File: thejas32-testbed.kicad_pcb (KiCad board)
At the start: 4 copper layers, 81.4 x 89.2 mm, 101 parts, among them J1 Conn_01x04, J10 Conn_02x10_Odd_Even, J11 Conn_01x03, J12 Conn_02x20_Odd_Even, J13 Conn_01x03, J2 USB_B_Micro, J3 Conn_02x03_Odd_Even, J4 Conn_02x05_Odd_Even, J5 Conn_01x05, J6 Conn_01x10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

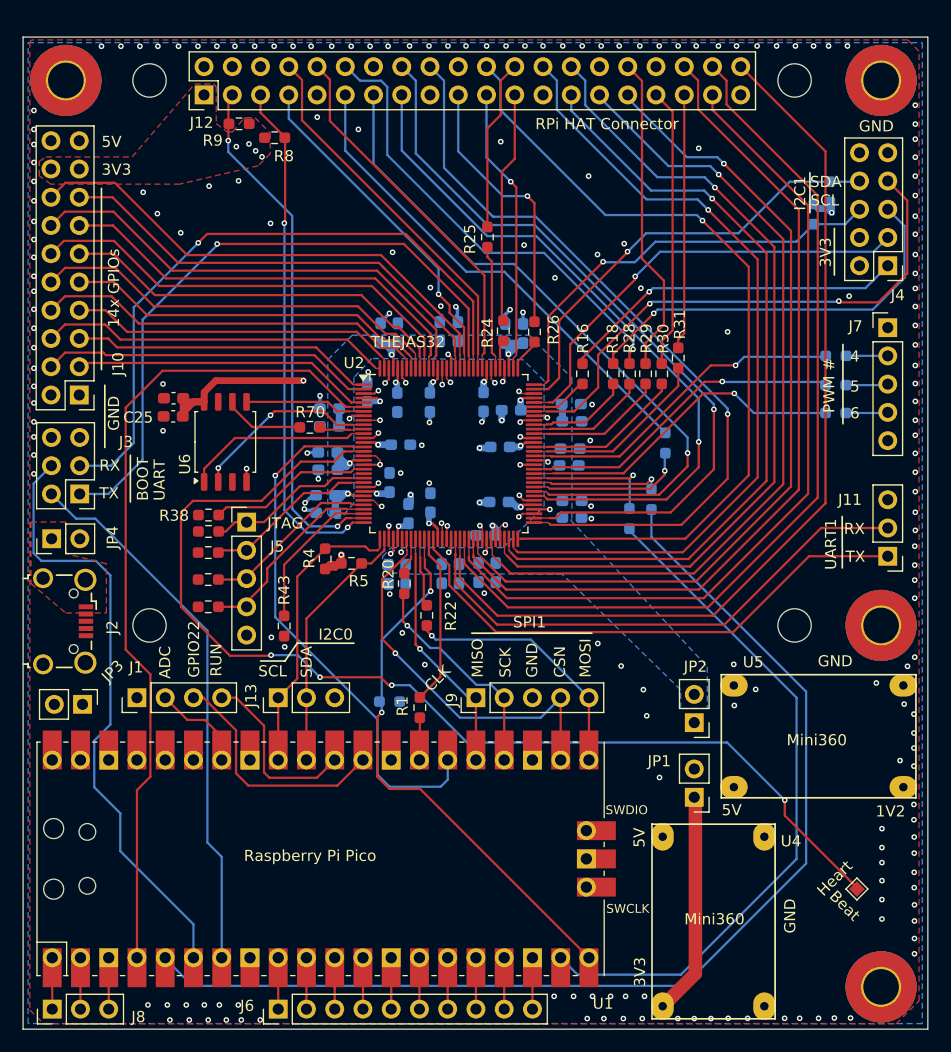
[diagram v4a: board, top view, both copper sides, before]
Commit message: Align Pico USB connector to board edge
Also moved J8, J6 and J9 to the left to match the Pico.
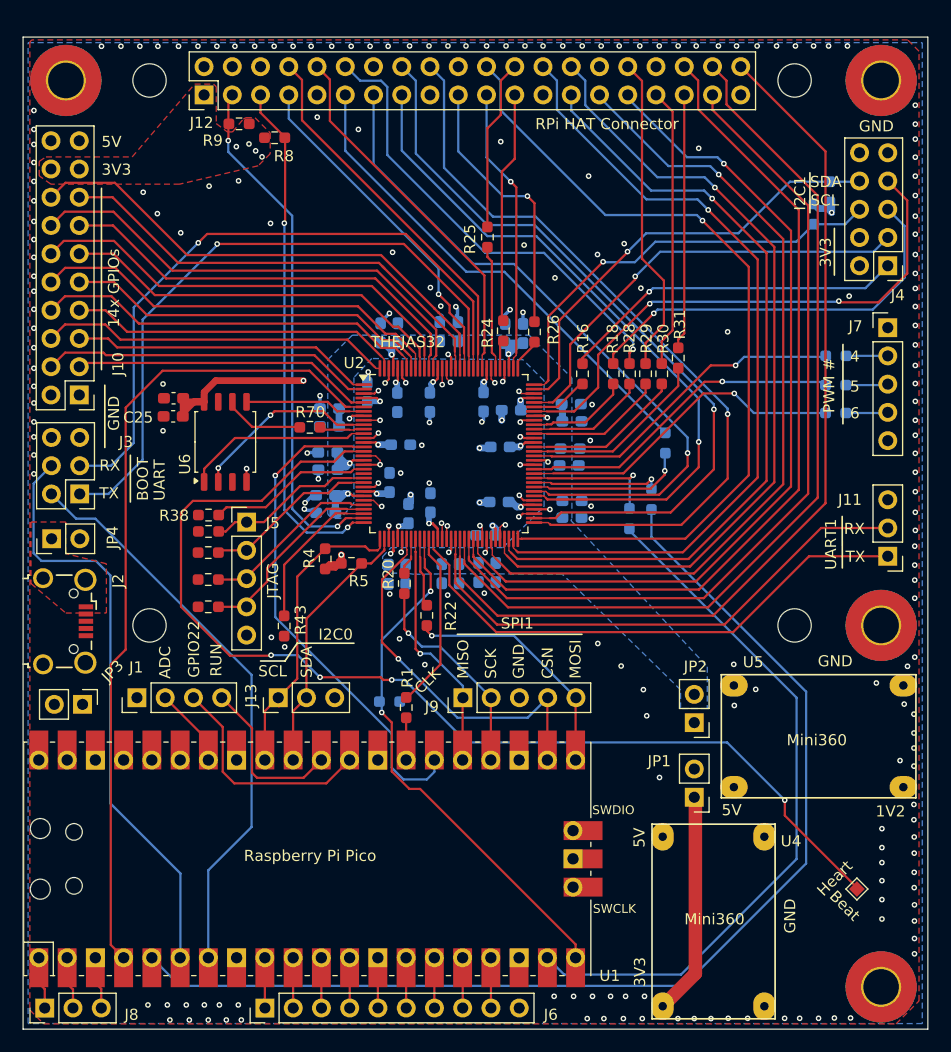
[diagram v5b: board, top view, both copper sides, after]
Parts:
- moved R1 1.23 mm to (151.7, 126.9)
- moved U1 1.20 mm to (142.8, 140.5)
- moved J6 1.19 mm to (139.0, 153.9)
- moved J9 1.17 mm to (156.8, 126.0)
- moved J8 0.68 mm to (119.2, 153.9)
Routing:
- net GND: track 70.8 -> 66.3 mm, vias 233 -> 232
- net MCU_BOOT_SEL: track 48.5 -> 45.3 mm
- net MCU_BOOT_UART_TX_PICO: track 49.1 -> 51.8 mm
- net MCU_RESETN: track 49.4 -> 47.5 mm
- net MCU_BOOT_UART_RX_PICO: track 54.9 -> 53.3 mm
- net MCU_SPI1_SCK: track 20.8 -> 19.2 mm
- net MCU_SPI1_CSN: track 35.7 -> 34.3 mm
- net Net-(J1-Pin_2): track 8.62 -> 7.21 mm
- net Net-(J1-Pin_4): track 16.3 -> 15.0 mm
- net Net-(J1-Pin_3): track 21.7 -> 20.5 mm
- net MCU_PWM_7: track 62.1 -> 63.3 mm
- net MCU_GPIO_00: track 100.9 -> 102.0 mm
- net MCU_SPI1_MOSI: track 23.1 -> 22.0 mm

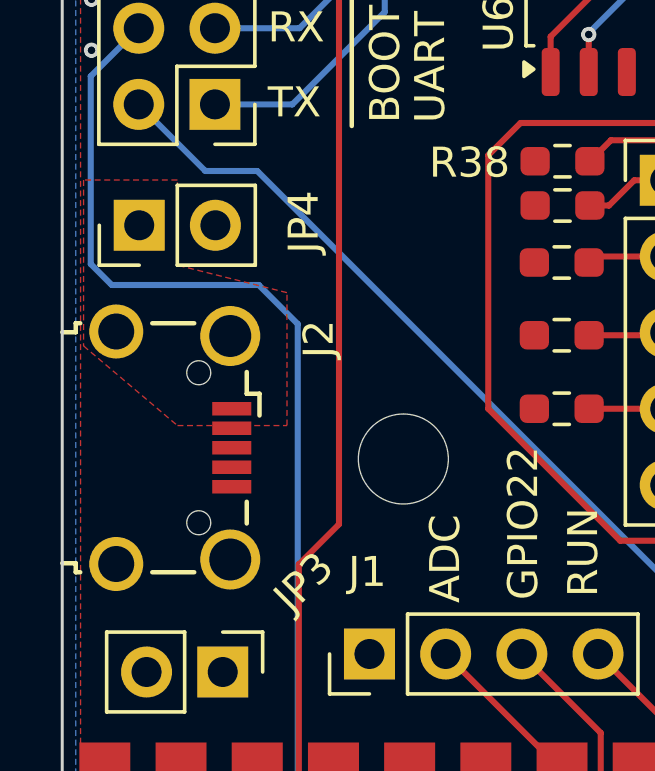
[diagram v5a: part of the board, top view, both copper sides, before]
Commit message: USB footprint changed to Molex-105017-0001
This component is very close to Sunrom Part 4653

https://www.sunrom.com/p/microusb-connector-with-through-hole-support-legs

I am using the footprint from Molex, but the board
will use the Sunrom part.
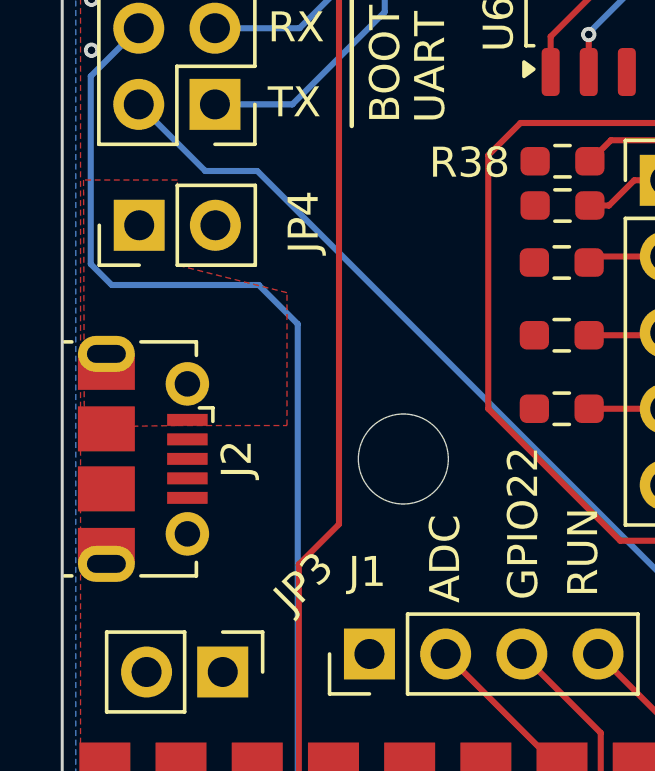
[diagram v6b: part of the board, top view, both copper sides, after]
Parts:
- J2: footprint Connector_USB:USB_Micro-B_Wuerth_629105150521_CircularHoles -> Connector_USB:USB_Micro-B_Molex-105017-0001
- moved J2 1.11 mm to (120.0, 119.5)

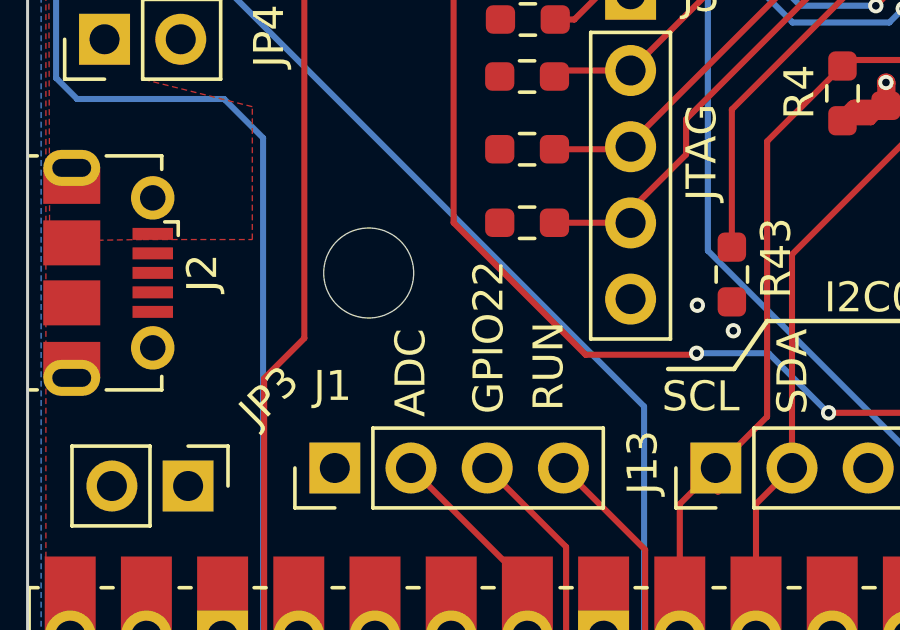
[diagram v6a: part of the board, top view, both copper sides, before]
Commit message: Fix silkscreen for GPIO pin
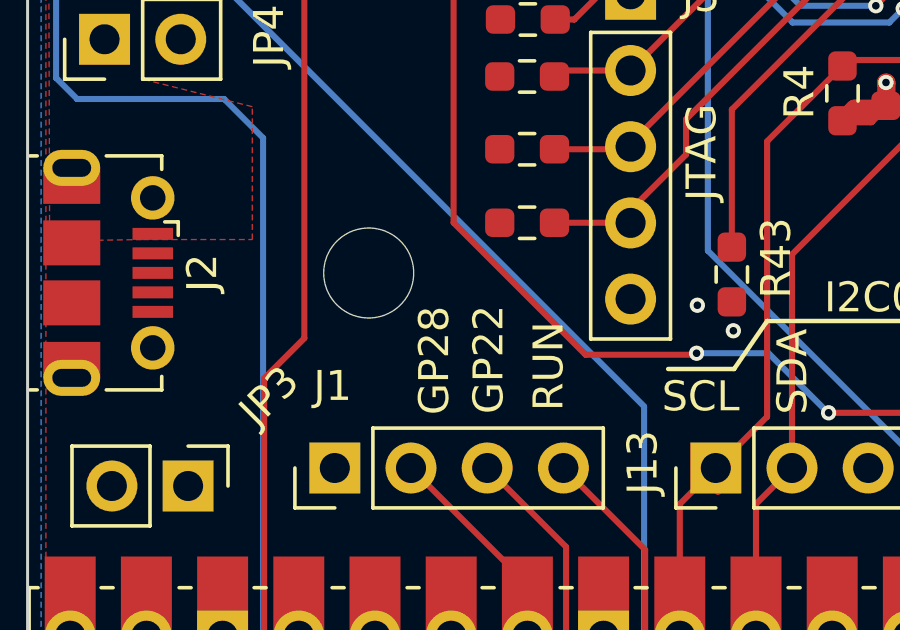
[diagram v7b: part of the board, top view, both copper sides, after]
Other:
- board text added: "GP22"
- board text added: "GP28"
- board text removed: "ADC"
- board text removed: "GPIO22"
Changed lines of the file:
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@@
 		)
 	)
-	(gr_text "GPIO22"
+	(gr_text "GP22"
 		(at 133.2 124.2 90)
 		(layer "F.SilkS")
@@
 		)
 	)
-	(gr_text "ADC"
-		(at 130.6 124.3 90)
-		(layer "F.SilkS")
-		(effects
+	(gr_text "GP28"
+		(at 131.388653 124.233651 90)
+		(layer "F.SilkS")
+		(effects
